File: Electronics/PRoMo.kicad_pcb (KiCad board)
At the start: 2 copper layers, 0 parts

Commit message: Schematic update and placement DONE
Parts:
- added C1: 100nF, Capacitor_SMD:C_0805_2012Metric_Pad1.15x1.40mm_HandSolder, F.Cu at (160.5, 68.3)
- added C10: 100nF, Capacitor_SMD:C_0805_2012Metric_Pad1.15x1.40mm_HandSolder, F.Cu at (151.2, 92.5)
- added C11: 10uF, Capacitor_SMD:C_0805_2012Metric_Pad1.15x1.40mm_HandSolder, F.Cu at (151.0, 98.0)
- added C12: 1uF, Capacitor_SMD:C_0805_2012Metric_Pad1.15x1.40mm_HandSolder, F.Cu at (145.3, 84.6)
- added C13: 100nF, Capacitor_SMD:C_0805_2012Metric_Pad1.15x1.40mm_HandSolder, F.Cu at (146.7, 83.1)
- added C14: 4.7uF, Capacitor_SMD:C_0805_2012Metric_Pad1.15x1.40mm_HandSolder, F.Cu at (132.7, 86.8)
- added C15: 100uF, Capacitor_THT:CP_Radial_D6.3mm_P2.50mm, F.Cu at (179.0, 91.8)
- added C16: 100nF, Capacitor_SMD:C_0805_2012Metric_Pad1.15x1.40mm_HandSolder, F.Cu at (180.0, 86.5)
- added C18: 100nF, Capacitor_SMD:C_0805_2012Metric_Pad1.15x1.40mm_HandSolder, F.Cu at (186.4, 134.8)
- added C2: 18pF, Capacitor_SMD:C_0805_2012Metric_Pad1.15x1.40mm_HandSolder, F.Cu at (156.5, 88.9)
- added C20: 100nF, Capacitor_SMD:C_0805_2012Metric_Pad1.15x1.40mm_HandSolder, F.Cu at (99.7, 131.6)
- added C22: 100nF, Capacitor_SMD:C_0805_2012Metric_Pad1.15x1.40mm_HandSolder, F.Cu at (99.7, 89.3)
- added C26: 10nF, Capacitor_SMD:C_0805_2012Metric_Pad1.15x1.40mm_HandSolder, F.Cu at (136.5, 112.3)
- added C27: 100nF, Capacitor_SMD:C_0805_2012Metric_Pad1.15x1.40mm_HandSolder, F.Cu at (144.5, 112.3)
- added C28: 100nF, Capacitor_SMD:C_0805_2012Metric_Pad1.15x1.40mm_HandSolder, F.Cu at (140.5, 114.0)
- added C29: 2.2nF, Capacitor_SMD:C_0805_2012Metric_Pad1.15x1.40mm_HandSolder, F.Cu at (144.5, 108.3)
- added C3: 18pF, Capacitor_SMD:C_0805_2012Metric_Pad1.15x1.40mm_HandSolder, F.Cu at (156.4, 86.4)
- added C30: 10nF, Capacitor_SMD:C_0805_2012Metric_Pad1.15x1.40mm_HandSolder, F.Cu at (143.0, 120.5)
- added C31: 2.2uF, Capacitor_SMD:C_0805_2012Metric_Pad1.15x1.40mm_HandSolder, F.Cu at (139.2, 120.5)
- added C32: 10uF, Capacitor_SMD:C_0805_2012Metric_Pad1.15x1.40mm_HandSolder, F.Cu at (140.9, 118.5)
- added C33: 680uF, Capacitor_THT:CP_Radial_D6.3mm_P2.50mm, F.Cu at (177.2, 133.3)
- added C34: 220uF, Capacitor_THT:CP_Radial_D6.3mm_P2.50mm, F.Cu at (161.2, 133.3)
- added C35: 10uF, Capacitor_Tantalum_SMD:CP_EIA-3216-18_Kemet-A_Pad1.58x1.35mm_HandSolder, F.Cu at (157.2, 128.1)
- added C36: 100uF, Capacitor_THT:CP_Radial_D6.3mm_P2.50mm, F.Cu at (121.4, 126.8)
- added C37: 100nF, Capacitor_SMD:C_0805_2012Metric_Pad1.15x1.40mm_HandSolder, F.Cu at (122.2, 146.8)
- added C38: Unpopulated, Capacitor_SMD:C_0805_2012Metric_Pad1.15x1.40mm_HandSolder, F.Cu at (126.0, 120.8)
- added C39: 100nF, Capacitor_SMD:C_0805_2012Metric_Pad1.15x1.40mm_HandSolder, F.Cu at (110.0, 142.3)
- added C4: 100nF, Capacitor_SMD:C_0805_2012Metric_Pad1.15x1.40mm_HandSolder, F.Cu at (136.2, 83.8)
- added C40: 4.7uF, Capacitor_SMD:C_0805_2012Metric_Pad1.15x1.40mm_HandSolder, F.Cu at (122.2, 142.8)
- added C5: 100nF, Capacitor_SMD:C_0805_2012Metric_Pad1.15x1.40mm_HandSolder, F.Cu at (140.0, 102.1)
- added C6: 2.2uF, Capacitor_SMD:C_0805_2012Metric_Pad1.15x1.40mm_HandSolder, F.Cu at (130.5, 86.8)
- added C7: 100nF, Capacitor_SMD:C_0805_2012Metric_Pad1.15x1.40mm_HandSolder, F.Cu at (130.5, 91.3)
- added C8: 2.2uF, Capacitor_SMD:C_0805_2012Metric_Pad1.15x1.40mm_HandSolder, F.Cu at (137.0, 102.3)
- added C9: 100nF, Capacitor_SMD:C_0805_2012Metric_Pad1.15x1.40mm_HandSolder, F.Cu at (149.5, 96.5)
- added D1: LED_Blue, LED_SMD:LED_0805_2012Metric_Pad1.15x1.40mm_HandSolder, F.Cu at (118.0, 65.5)
- added D10: SK6812, LED_SMD:LED_SK6812_PLCC4_5.0x5.0mm_P3.2mm, F.Cu at (95.0, 89.5)
- added D14: SS14, Diode_SMD:D_SMA_Handsoldering, F.Cu at (176.2, 125.8)
- added D15: LED_Red, LED_SMD:LED_0805_2012Metric_Pad1.15x1.40mm_HandSolder, F.Cu at (165.2, 151.1)
- added D16: LED_Yellow, LED_SMD:LED_0805_2012Metric_Pad1.15x1.40mm_HandSolder, F.Cu at (124.5, 150.8)
- added D17: LED_Green, LED_SMD:LED_0805_2012Metric_Pad1.15x1.40mm_HandSolder, F.Cu at (160.7, 151.1)
- added D18: LED_Green, LED_SMD:LED_0805_2012Metric_Pad1.15x1.40mm_HandSolder, F.Cu at (156.2, 151.1)
- added D19: D_Zener_Small, Diode_SMD:D_SMA_Handsoldering, F.Cu at (106.7, 146.1)
- added D2: LED_Blue, LED_SMD:LED_0805_2012Metric_Pad1.15x1.40mm_HandSolder, F.Cu at (120.0, 65.5)
- added D20: Yellow, LED_SMD:LED_0805_2012Metric_Pad1.15x1.40mm_HandSolder, F.Cu at (114.7, 150.8)
- added D21: Yellow, LED_SMD:LED_0805_2012Metric_Pad1.15x1.40mm_HandSolder, F.Cu at (117.0, 150.8)
- added D3: M7, Diode_SMD:D_SMA_Handsoldering, F.Cu at (179.9, 88.5)
- added D4: SK6812, LED_SMD:LED_SK6812_PLCC4_5.0x5.0mm_P3.2mm, F.Cu at (186.2, 89.8)
- added D6: SK6812, LED_SMD:LED_SK6812_PLCC4_5.0x5.0mm_P3.2mm, F.Cu at (186.2, 130.8)
- added D8: SK6812, LED_SMD:LED_SK6812_PLCC4_5.0x5.0mm_P3.2mm, F.Cu at (95.0, 131.1)
- added H1: MountingHole, MountingHole:MountingHole_2.7mm_M2.5, F.Cu at (115.1, 97.6)
- added H2: MountingHole, MountingHole:MountingHole_2.7mm_M2.5, F.Cu at (158.2, 77.3)
- added H3: MountingHole, MountingHole:MountingHole_2.7mm_M2.5, F.Cu at (150.6, 128.1)
- added H4: MountingHole, MountingHole:MountingHole_2.7mm_M2.5, F.Cu at (130.9, 128.1)
- added J1: AN14, Connector_PinHeader_2.54mm:PinHeader_1x03_P2.54mm_Vertical, F.Cu at (125.2, 81.8)
- added J10: SPI1_AUX, Connector_PinHeader_2.54mm:PinHeader_1x06_P2.54mm_Vertical, F.Cu at (110.0, 81.8)
- added J11: I2C2_AUX, Connector_PinHeader_2.54mm:PinHeader_1x04_P2.54mm_Vertical, F.Cu at (115.1, 81.8)
- added J12: Conn_01x02, Connector_PinHeader_2.54mm:PinHeader_1x02_P2.54mm_Vertical, F.Cu at (98.0, 80.8)
- added J13: Conn_01x02, Connector_PinHeader_2.54mm:PinHeader_1x02_P2.54mm_Vertical, F.Cu at (150.5, 65.8)
- added J14: Conn_01x02, Connector_PinHeader_2.54mm:PinHeader_1x02_P2.54mm_Vertical, F.Cu at (183.5, 80.8)
- added J15: Conn_01x02, Connector_PinHeader_2.54mm:PinHeader_1x02_P2.54mm_Vertical, F.Cu at (150.7, 154.3)
- added J16: ME_L, Connector_PinHeader_2.54mm:PinHeader_1x06_P2.54mm_Vertical, F.Cu at (131.6, 116.7)
- added J17: ME_R, Connector_PinHeader_2.54mm:PinHeader_1x06_P2.54mm_Vertical, F.Cu at (149.4, 116.7)
- added J18: Conn_01x02, Connector_PinHeader_2.54mm:PinHeader_1x02_P2.54mm_Vertical, F.Cu at (157.2, 141.3)
- added J19: Conn_02x02_Counter_Clockwise, Connector_PinSocket_2.54mm:PinSocket_2x02_P2.54mm_Vertical, F.Cu at (153.5, 134.6)
- added J2: GPIO1, Connector_PinHeader_2.54mm:PinHeader_1x03_P2.54mm_Vertical, F.Cu at (168.4, 95.0)
- added J20: Conn_02x02_Counter_Clockwise, Connector_PinSocket_2.54mm:PinSocket_2x02_P2.54mm_Vertical, F.Cu at (130.8, 134.6)
- added J21: AUX_IN, Connector_PinHeader_2.54mm:PinHeader_1x02_P2.54mm_Vertical, F.Cu at (176.7, 141.3)
- added J22: AUX_OUT, Connector_PinHeader_2.54mm:PinHeader_1x02_P2.54mm_Vertical, F.Cu at (161.7, 141.3)
- added J23: USB_B_Micro, Connector_USB:USB_Micro-B_Molex_47346-0001, F.Cu at (122.7, 157.6)
- added J24: Conn_01x02, Connector_PinHeader_2.54mm:PinHeader_1x02_P2.54mm_Vertical, F.Cu at (109.0, 137.8)
- added J3: GPIO2, Connector_PinHeader_2.54mm:PinHeader_1x03_P2.54mm_Vertical, F.Cu at (168.4, 84.9)
- added J4: GPIO3, Connector_PinHeader_2.54mm:PinHeader_1x03_P2.54mm_Vertical, F.Cu at (168.4, 74.7)
- added J5: AN8, Connector_PinHeader_2.54mm:PinHeader_1x03_P2.54mm_Vertical, F.Cu at (108.7, 127.8)
- added J6: AN9, Connector_PinHeader_2.54mm:PinHeader_1x03_P2.54mm_Vertical, F.Cu at (103.6, 127.8)
- added J7: AN15, Connector_PinHeader_2.54mm:PinHeader_1x03_P2.54mm_Vertical, F.Cu at (120.1, 81.8)
- added J8: Programming, Connector_PinHeader_2.54mm:PinHeader_1x06_P2.54mm_Vertical, F.Cu at (173.5, 79.8)
- added J9: UART6_AUX, Connector_PinHeader_2.54mm:PinHeader_1x06_P2.54mm_Vertical, F.Cu at (104.9, 81.8)
- added JP1: SolderJumper_3_Bridged12, Jumper:SolderJumper-3_P1.3mm_Bridged12_Pad1.0x1.5mm, F.Cu at (125.2, 77.3)
- added JP10: SolderJumper_3_Bridged12, Jumper:SolderJumper-3_P1.3mm_Bridged12_Pad1.0x1.5mm, F.Cu at (120.2, 77.3)
- added JP11: SolderJumper_2_Bridged, Jumper:SolderJumper-2_P1.3mm_Bridged_Pad1.0x1.5mm, F.Cu at (121.2, 90.7)
- added JP12: SolderJumper_2_Open, Jumper:SolderJumper-2_P1.3mm_Open_Pad1.0x1.5mm, B.Cu at (137.0, 92.3)
- added JP13: SolderJumper_2_Open, Jumper:SolderJumper-2_P1.3mm_Open_Pad1.0x1.5mm, B.Cu at (140.5, 95.8)
- added JP14: SolderJumper_2_Bridged, Jumper:SolderJumper-2_P1.3mm_Bridged_Pad1.0x1.5mm, F.Cu at (96.2, 84.0)
- added JP15: SolderJumper_2_Bridged, Jumper:SolderJumper-2_P1.3mm_Bridged_Pad1.0x1.5mm, B.Cu at (150.7, 72.0)
- added JP16: SolderJumper_2_Bridged, Jumper:SolderJumper-2_P1.3mm_Bridged_Pad1.0x1.5mm, F.Cu at (185.2, 84.0)
- added JP17: SolderJumper_2_Bridged, Jumper:SolderJumper-2_P1.3mm_Bridged_Pad1.0x1.5mm, B.Cu at (150.1, 157.6)
- added JP18: SolderJumper_2_Bridged, Jumper:SolderJumper-2_P1.3mm_Bridged_Pad1.0x1.5mm, F.Cu at (120.7, 68.8)
- added JP19: SolderJumper_2_Bridged, Jumper:SolderJumper-2_P1.3mm_Bridged_Pad1.0x1.5mm, F.Cu at (125.2, 71.5)
- added JP2: SolderJumper_3_Bridged12, Jumper:SolderJumper-3_P1.3mm_Bridged12_Pad1.0x1.5mm, F.Cu at (164.6, 95.0)
- added JP20: SolderJumper_2_Bridged, Jumper:SolderJumper-2_P1.3mm_Bridged_Pad1.0x1.5mm, F.Cu at (117.0, 68.8)
- added JP21: SolderJumper_2_Bridged, Jumper:SolderJumper-2_P1.3mm_Bridged_Pad1.0x1.5mm, F.Cu at (133.5, 120.7)
- added JP22: SolderJumper_2_Bridged, Jumper:SolderJumper-2_P1.3mm_Bridged_Pad1.0x1.5mm, F.Cu at (136.0, 120.7)
- added JP23: SolderJumper_3_Bridged12, Jumper:SolderJumper-3_P1.3mm_Bridged12_Pad1.0x1.5mm, F.Cu at (110.0, 77.3)
- added JP24: SolderJumper_3_Bridged12, Jumper:SolderJumper-3_P1.3mm_Bridged12_Pad1.0x1.5mm, F.Cu at (115.1, 77.3)
- added JP25: SLAVE_ADDR, Jumper:SolderJumper-3_P1.3mm_Bridged12_Pad1.0x1.5mm, F.Cu at (136.2, 108.0)
- added JP26: SolderJumper_2_Bridged, Jumper:SolderJumper-2_P1.3mm_Bridged_Pad1.0x1.5mm, F.Cu at (136.9, 134.7)
- added JP27: SolderJumper_2_Bridged, Jumper:SolderJumper-2_P1.3mm_Bridged_Pad1.0x1.5mm, F.Cu at (144.9, 134.6)
- added JP3: SolderJumper_3_Bridged12, Jumper:SolderJumper-3_P1.3mm_Bridged12_Pad1.0x1.5mm, F.Cu at (164.6, 84.9)
- added JP4: SolderJumper_3_Bridged12, Jumper:SolderJumper-3_P1.3mm_Bridged12_Pad1.0x1.5mm, F.Cu at (164.6, 74.7)
- added JP5: SolderJumper_3_Bridged12, Jumper:SolderJumper-3_P1.3mm_Bridged12_Pad1.0x1.5mm, F.Cu at (108.7, 124.8)
- added JP6: SolderJumper_3_Bridged12, Jumper:SolderJumper-3_P1.3mm_Bridged12_Pad1.0x1.5mm, F.Cu at (103.7, 124.8)
- added JP7: SolderJumper_2_Bridged, Jumper:SolderJumper-2_P1.3mm_Bridged_Pad1.0x1.5mm, F.Cu at (124.2, 90.7)
- added JP8: SolderJumper_2_Bridged, Jumper:SolderJumper-2_P1.3mm_Bridged_Pad1.0x1.5mm, F.Cu at (114.2, 131.3)
- added JP9: SolderJumper_2_Bridged, Jumper:SolderJumper-2_P1.3mm_Bridged_Pad1.0x1.5mm, F.Cu at (98.2, 137.3)
- added L1: 22uh, Inductor_SMD:L_0805_2012Metric_Pad1.15x1.40mm_HandSolder, F.Cu at (166.7, 125.4)
- added L2: 33uh, Inductor_SMD:L_7.3x7.3_H3.5, F.Cu at (166.8, 125.4)
- added R1: 1k, Resistor_SMD:R_0805_2012Metric_Pad1.15x1.40mm_HandSolder, F.Cu at (126.5, 90.8)
- added R10: 1k, Resistor_SMD:R_0805_2012Metric_Pad1.15x1.40mm_HandSolder, F.Cu at (120.2, 93.8)
- added R11: 10k, Resistor_SMD:R_0805_2012Metric_Pad1.15x1.40mm_HandSolder, F.Cu at (152.5, 99.5)
- added R12: 47, Resistor_SMD:R_0805_2012Metric_Pad1.15x1.40mm_HandSolder, F.Cu at (116.0, 65.5)
- added R13: 47, Resistor_SMD:R_0805_2012Metric_Pad1.15x1.40mm_HandSolder, F.Cu at (122.0, 65.5)
- added R14: 10k, Resistor_SMD:R_0805_2012Metric_Pad1.15x1.40mm_HandSolder, F.Cu at (121.5, 71.5)
- added R15: 1k, Resistor_SMD:R_0805_2012Metric_Pad1.15x1.40mm_HandSolder, F.Cu at (124.8, 45.0)
- added R16: 1k, Resistor_SMD:R_0805_2012Metric_Pad1.15x1.40mm_HandSolder, F.Cu at (124.8, 42.4)
- added R17: 1k, Resistor_SMD:R_0805_2012Metric_Pad1.15x1.40mm_HandSolder, F.Cu at (125.0, 39.3)
- added R18: Sense, Resistor_SMD:R_2512_6332Metric_Pad1.52x3.35mm_HandSolder, F.Cu at (136.7, 134.8)
- added R19: Sense, Resistor_SMD:R_2512_6332Metric_Pad1.52x3.35mm_HandSolder, F.Cu at (145.0, 134.7)
- added R2: 1k, Resistor_SMD:R_0805_2012Metric_Pad1.15x1.40mm_HandSolder, F.Cu at (111.7, 131.3)
- added R20: 47k, Resistor_SMD:R_0805_2012Metric_Pad1.15x1.40mm_HandSolder, F.Cu at (136.7, 127.8)
- added R21: 470, Resistor_SMD:R_0805_2012Metric_Pad1.15x1.40mm_HandSolder, F.Cu at (167.5, 151.0)
- added R22: 330, Resistor_SMD:R_0805_2012Metric_Pad1.15x1.40mm_HandSolder, F.Cu at (126.7, 150.8)
- added R23: 220, Resistor_SMD:R_0805_2012Metric_Pad1.15x1.40mm_HandSolder, F.Cu at (163.0, 151.1)
- added R24: 47, Resistor_SMD:R_0805_2012Metric_Pad1.15x1.40mm_HandSolder, F.Cu at (158.5, 151.1)
- added R25: 220, Resistor_SMD:R_0805_2012Metric_Pad1.15x1.40mm_HandSolder, F.Cu at (112.5, 150.8)
- added R26: 220, Resistor_SMD:R_0805_2012Metric_Pad1.15x1.40mm_HandSolder, F.Cu at (110.2, 150.8)
- added R3: 1k, Resistor_SMD:R_0805_2012Metric_Pad1.15x1.40mm_HandSolder, F.Cu at (100.7, 137.3)
- added R4: 1k, Resistor_SMD:R_0805_2012Metric_Pad1.15x1.40mm_HandSolder, F.Cu at (124.9, 93.8)
- added R5: 1k, Resistor_SMD:R_0805_2012Metric_Pad1.15x1.40mm_HandSolder, F.Cu at (113.0, 134.3)
- added R6: 1k, Resistor_SMD:R_0805_2012Metric_Pad1.15x1.40mm_HandSolder, F.Cu at (99.2, 140.3)
- added R7: 1k, Resistor_SMD:R_0805_2012Metric_Pad1.15x1.40mm_HandSolder, F.Cu at (119.0, 90.8)
- added R8: Unpopulated, Resistor_SMD:R_0805_2012Metric_Pad1.15x1.40mm_HandSolder, F.Cu at (162.5, 68.3)
- added R9: 1k, Resistor_SMD:R_0805_2012Metric_Pad1.15x1.40mm_HandSolder, F.Cu at (125.0, 48.2)
- added SW1: RESET_BP, Button_Switch_THT:SW_TH_Tactile_Omron_B3F-10xx, F.Cu at (153.7, 69.0)
- added SW2: WKP_BP, Button_Switch_THT:SW_TH_Tactile_Omron_B3F-10xx, F.Cu at (124.7, 69.0)
- added SW3: SW_SPDT, Button_Switch_SMD:SW_SPDT_PCM12, F.Cu at (158.5, 157.8)
- added TP1: TestPoint, TestPoint:TestPoint_Pad_D1.5mm, F.Cu at (132.7, 83.3)
- added TP2: TestPoint, TestPoint:TestPoint_Pad_D1.5mm, F.Cu at (147.0, 69.3)
- added TP3: TestPoint, TestPoint:TestPoint_Pad_D1.5mm, F.Cu at (178.0, 79.8)
- added TP4: TestPoint, TestPoint:TestPoint_Pad_D1.5mm, F.Cu at (147.5, 151.3)
- added TP5: TestPoint, TestPoint:TestPoint_Pad_D1.5mm, F.Cu at (124.2, 139.1)
- added TP6: TestPoint, TestPoint:TestPoint_Pad_D1.5mm, F.Cu at (124.2, 136.1)
- added U1: STM32F405RGTx, Package_QFP:LQFP-64_10x10mm_P0.5mm, F.Cu at (140.5, 92.3)
- added U10: NRF24L01_Breakout_alt, RF:nRF24L01_Breakout_alt, F.Cu at (123.0, 119.5)
- added U11: FT232RL, Package_SO:SSOP-28_5.3x10.2mm_P0.65mm, F.Cu at (116.0, 143.1)
- added U2: VL53l0x_breakout, Connector_PinSocket_2.54mm:PinSocket_1x06_P2.54mm_Vertical, F.Cu at (109.0, 68.8)
- added U3: VL53l0x_breakout, Connector_PinSocket_2.54mm:PinSocket_1x06_P2.54mm_Vertical, F.Cu at (134.0, 65.8)
- added U4: VL53l0x_breakout, Connector_PinSocket_2.54mm:PinSocket_1x06_P2.54mm_Vertical, F.Cu at (172.2, 69.1)
- added U5: VL53l0x_breakout, Connector_PinSocket_2.54mm:PinSocket_1x06_P2.54mm_Vertical, F.Cu at (134.3, 154.3)
- added U6: MPU-6050, Sensor_Motion:InvenSense_QFN-24_4x4mm_P0.5mm, F.Cu at (140.5, 110.3)
- added U7: DRV8833PWP, Package_SO:HTSSOP-16-1EP_4.4x5mm_P0.65mm_EP3.4x5mm_Mask2.46x2.31mm_ThermalVias, F.Cu at (140.8, 126.3)
- added U8: LM2596S-5, Package_TO_SOT_SMD:TO-263-5_TabPin3, F.Cu at (169.2, 138.3)
- added U9: AMS1117-3.3, Package_TO_SOT_SMD:SOT-223-3_TabPin2, F.Cu at (158.3, 122.3)
- added Y1: Crystal 25MHz, Crystal:Crystal_SMD_3225-4Pin_3.2x2.5mm_HandSoldering, F.Cu at (151.9, 87.6)
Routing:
- net GND: track 0.00 -> 0.71 mm
- added copper zone on B.Cu, net GND
- added copper zone on F.Cu, net GND
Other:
- board outline added: 100 x 100 mm

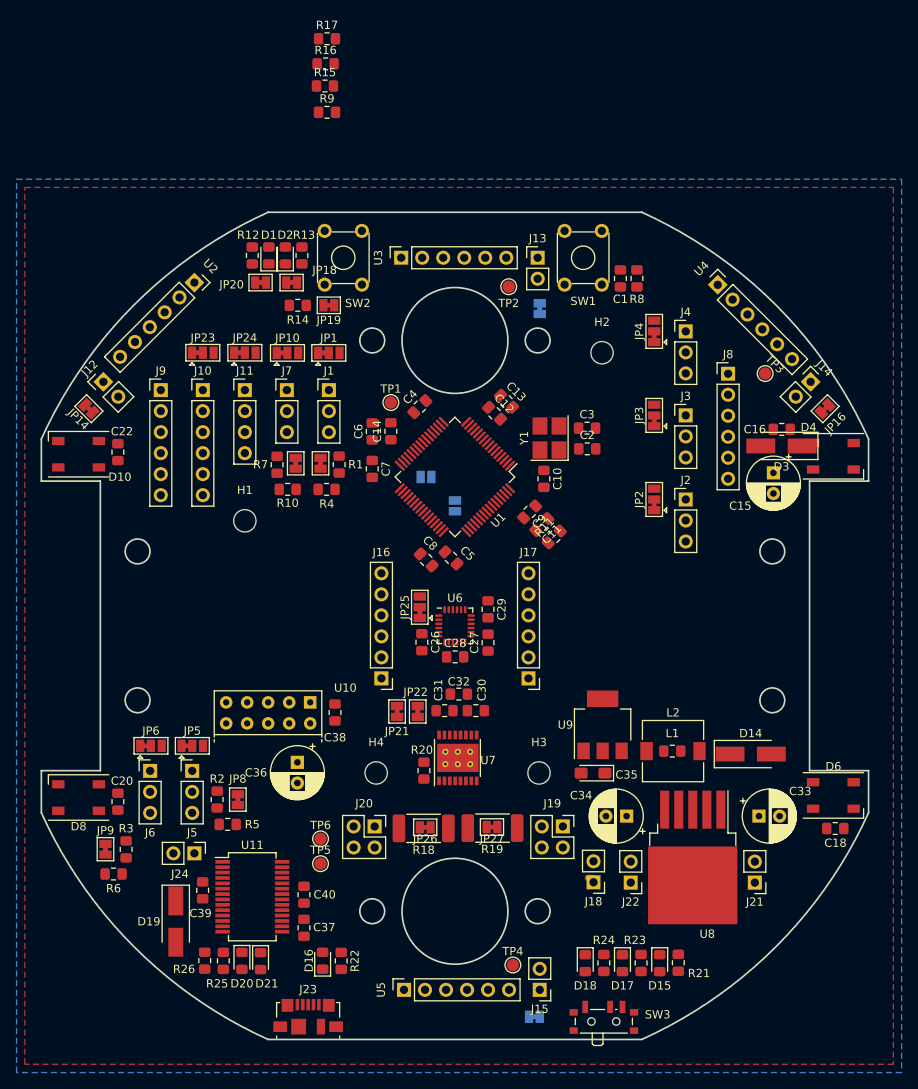
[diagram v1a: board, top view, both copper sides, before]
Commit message: Routing Done, All files ready for ordering
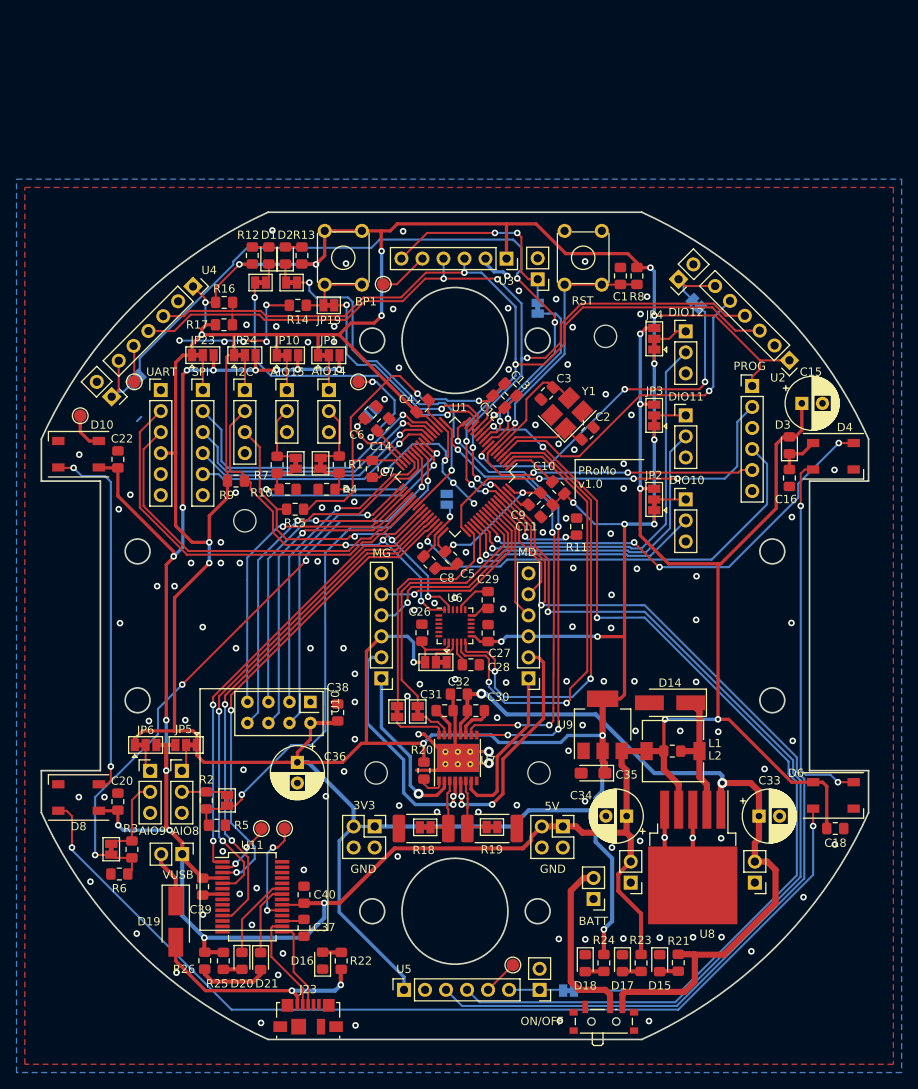
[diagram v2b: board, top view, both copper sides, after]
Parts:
- added TP7: TestPoint, TestPoint:TestPoint_Pad_D1.5mm, F.Cu at (95.2, 84.9)
- D3: footprint Diode_SMD:D_SMA_Handsoldering -> Diode_SMD:D_0805_2012Metric_Pad1.15x1.40mm_HandSolder
- JP14, JP16: moved to B.Cu
- R12, R13, R24: value 47 -> 47R
- R21: value 470 -> 470R
- R22: value 330 -> 330R
- R23, R25, R26: value 220 -> 220R
- U10: value NRF24L01_Breakout_alt -> NRF24L01_Breakout; footprint RF:nRF24L01_Breakout_alt -> RF_Module:nRF24L01_Breakout
- Y1: value Crystal 25MHz -> Crystal_GND24
- moved J14 84.5 mm to (99.0, 82.6), turned to 225 degrees
- moved JP16 83.4 mm to (101.9, 80.5), turned to 225 degrees
- moved TP3 76.3 mm to (101.7, 80.8), turned to 225 degrees
- moved JP14 74.5 mm to (169.6, 71.3)
- moved U2 72.5 mm to (180.9, 78.2), turned to 225 degrees
- moved J12 70.6 mm to (167.5, 68.4), turned to 135 degrees
- moved U4 63.4 mm to (108.8, 69.3), turned to 315 degrees
- moved R15 51.3 mm to (121.1, 96.2), turned to 180 degrees
- moved R9 45.9 mm to (114.0, 92.8)
- moved R17 36.8 mm to (112.5, 73.9)
- moved R16 31.3 mm to (112.6, 71.2)
- moved TP2 15.2 mm to (131.8, 69.0)
- moved U3 12.7 mm to (146.7, 65.9), turned to 270 degrees
- moved D14 11.6 mm to (166.5, 119.6), turned to 180 degrees
- moved JP12 10.3 mm to (130.3, 84.5), turned to 45 degrees
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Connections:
- U10 pad 1: +3V3 -> GND
- Y1 pad 2: Net-(C3-Pad1) -> GND
- Y1 pad 3: (no net) -> Net-(C3-Pad1)
- Y1 pad 4: (no net) -> GND
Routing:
- net +3V3: track 0.00 -> 608.5 mm, vias 0 -> 25
- net +5V: track 0.00 -> 358.4 mm, vias 0 -> 19
- net I2C1_SCL: track 0.00 -> 232.7 mm, vias 0 -> 6
- net I2C1_SDA: track 0.00 -> 228.0 mm, vias 0 -> 7
- net Net-(D6-Pad4): track 0.00 -> 118.4 mm, vias 0 -> 2
- net GND: track 0.71 -> 114.5 mm, vias 0 -> 140
- net Net-(JP17-Pad1): track 0.00 -> 109.7 mm, vias 0 -> 3
- net VBAT: track 0.00 -> 93.4 mm, vias 0 -> 2
- net Net-(JP16-Pad1): track 0.00 -> 84.8 mm, vias 0 -> 3
- net ADC1_9: track 0.00 -> 75.9 mm, vias 0 -> 4
- net /NRST: track 0.00 -> 66.9 mm, vias 0 -> 3
- net FTDI_CTS: track 0.00 -> 63.5 mm, vias 0 -> 2
- net ADC1_8: track 0.00 -> 63.3 mm, vias 0 -> 2
- net FTDI_RX: track 0.00 -> 60.2 mm, vias 0 -> 2
- net FTDI_RTS: track 0.00 -> 58.9 mm, vias 0 -> 2
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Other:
- board text added: "3V3"
- board text added: "5V"
- board text added: "AIO14"
- board text added: "AIO15"
- board text added: "AIO8"
- board text added: "AIO9"
- board text added: "BATT"
- board text added: "BP1"
- board text added: "DIO10"
- board text added: "DIO11"
- board text added: "DIO12"
- board text added: "GND"
- board text added: "I2C"
- board text added: "M1"
- board text added: "M2"
- board text added: "MD"
- board text added: "MG"
- board text added: "MI"
- board text added: "MO"
- board text added: "NSS"
- board text added: "ON/OFF"
- board text added: "PA"
- board text added: "PB"
- board text added: "PB0"
- board text added: "PB1"
- board text added: "PC10"
- board text added: "PC11"
- board text added: "PC12"
- board text added: "PC4"
- board text added: "PC5"
- board text added: "PROG"
- board text added: "PRoMo v1.0"
- board text added: "RST"
- board text added: "RX"
- board text added: "SCK"
- board text added: "SCL"
- board text added: "SDA"
- board text added: "SPI"
- board text added: "TCK"
- board text added: "TMS"
- board text added: "TX"
- board text added: "UART"
- board text added: "VCC"
- board text added: "VUSB"
